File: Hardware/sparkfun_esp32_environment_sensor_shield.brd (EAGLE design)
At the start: 58.4 x 50.8 mm, 51 parts, among them J1 WEATHER_METER-WIND, J2 WEATHER_METER-RAIN, U1 BME280, U2 CCS811, U3 TSL2561FN

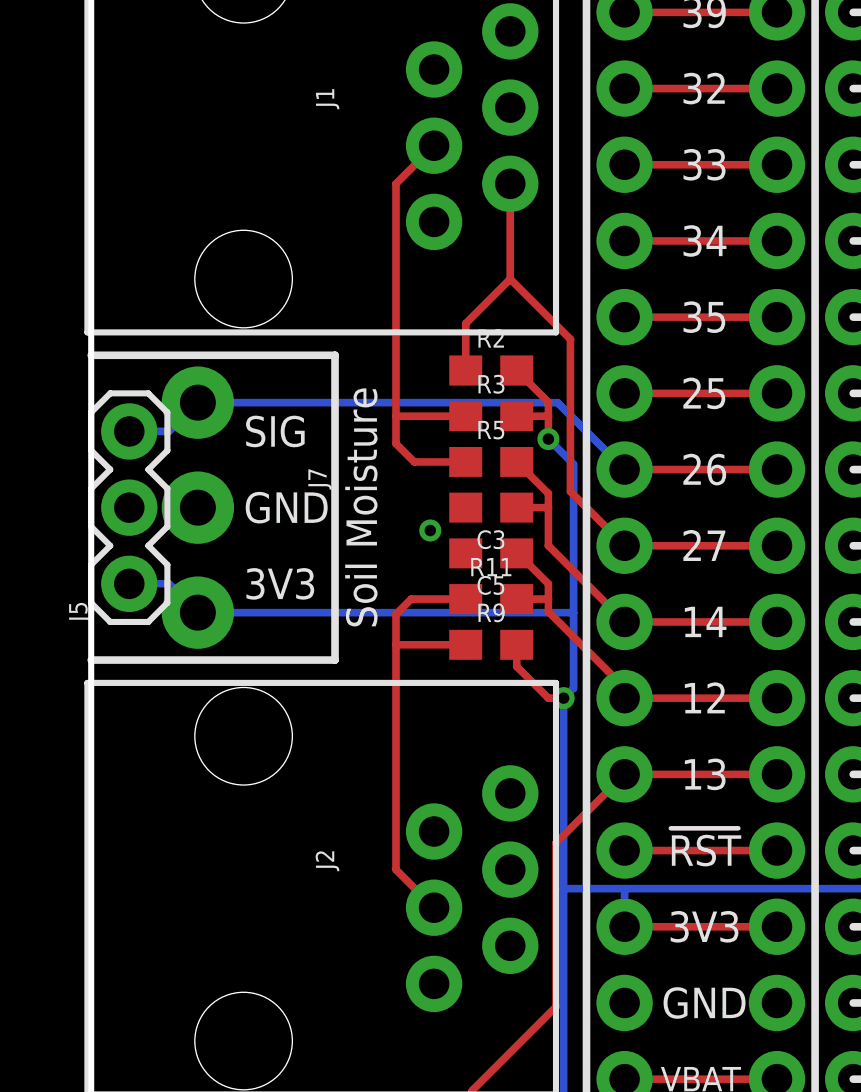
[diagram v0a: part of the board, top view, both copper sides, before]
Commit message: Revising weather meter circuits after tests with ESP32 Thing.
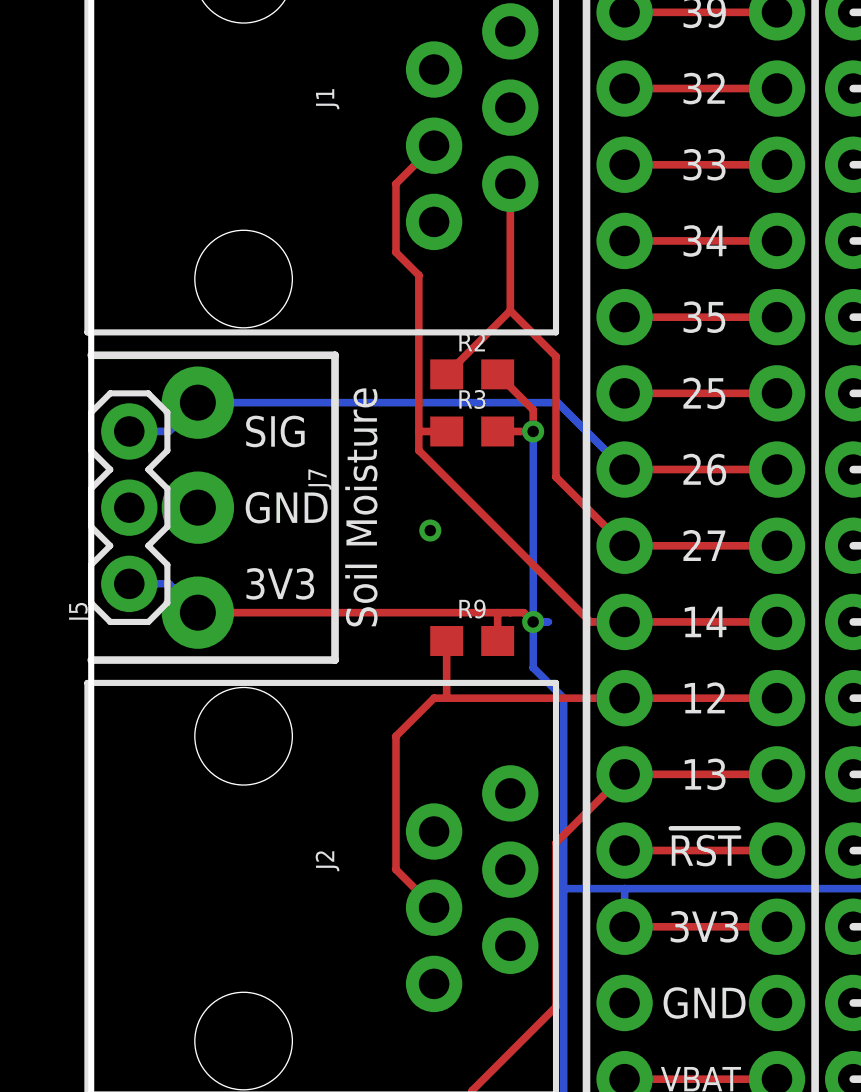
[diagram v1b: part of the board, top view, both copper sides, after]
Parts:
- removed C3, C5: 0.1uF, SparkFun-Capacitors:0603
- removed R11, R5: 330, SparkFun-Resistors:0603
- moved R3 0.81 mm to (12.7, 27.9)
- moved R2 0.65 mm to (12.7, 29.8)
- moved R9 0.65 mm to (12.7, 21.0)
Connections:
- removed net RAIN_OUT: J2.4, R11.1, R9.1
- removed net WIND_OUT: J1.4, R3.1, R5.1
- net GND: no longer C3.2, C5.2
- net RAINFALL: now also J2.4, R9.1; no longer C5.1, R11.2
- net WIND_SPEED: now also J1.4, R3.1; no longer C3.1, R5.2
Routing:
- net WIND_OUT: track 15.4 -> 0.00 mm
- net RAIN_OUT: track 15.2 -> 0.00 mm
- net WIND_SPEED: track 13.0 -> 26.2 mm
- net RAINFALL: track 12.5 -> 21.4 mm
- net 3.3V: track 212.6 -> 210.1 mm
- net WIND_DIR: track 22.4 -> 21.7 mm

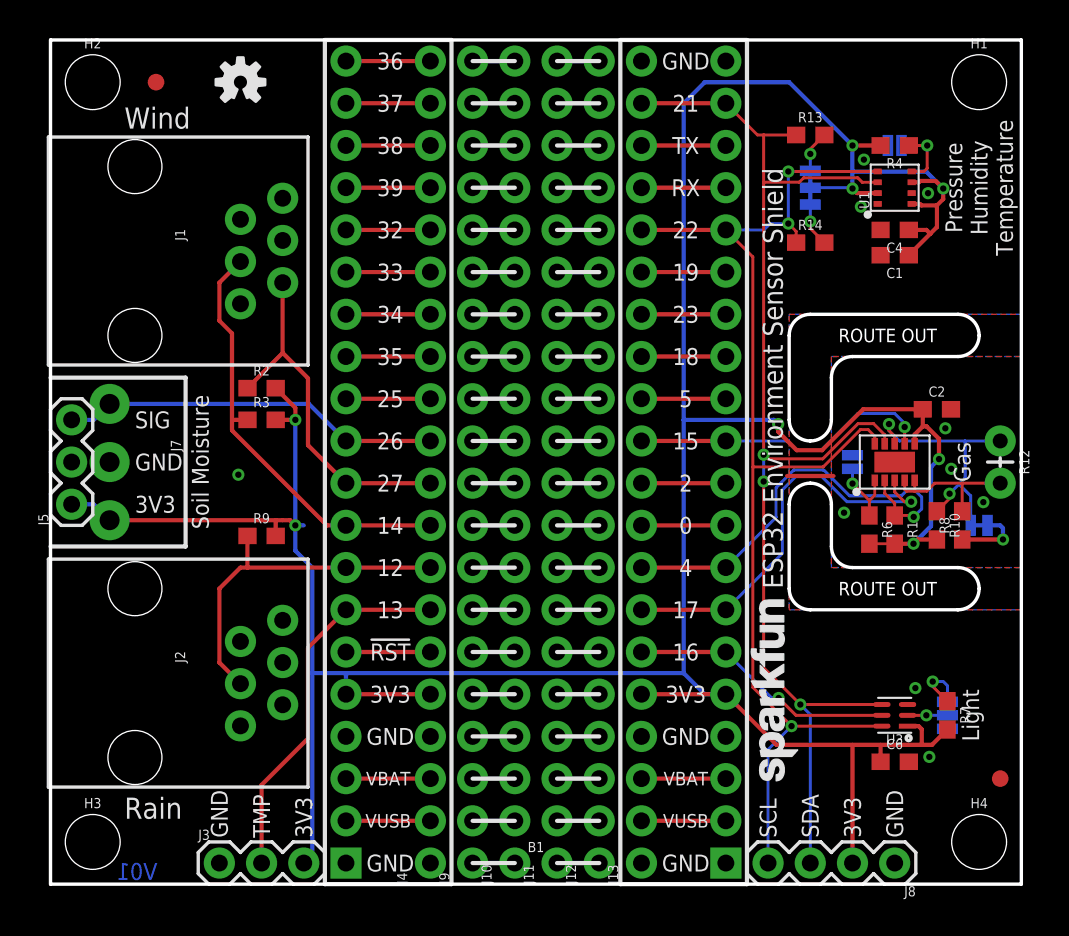
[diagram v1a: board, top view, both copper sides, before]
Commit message: Adding TVS diode to weather meter signals.
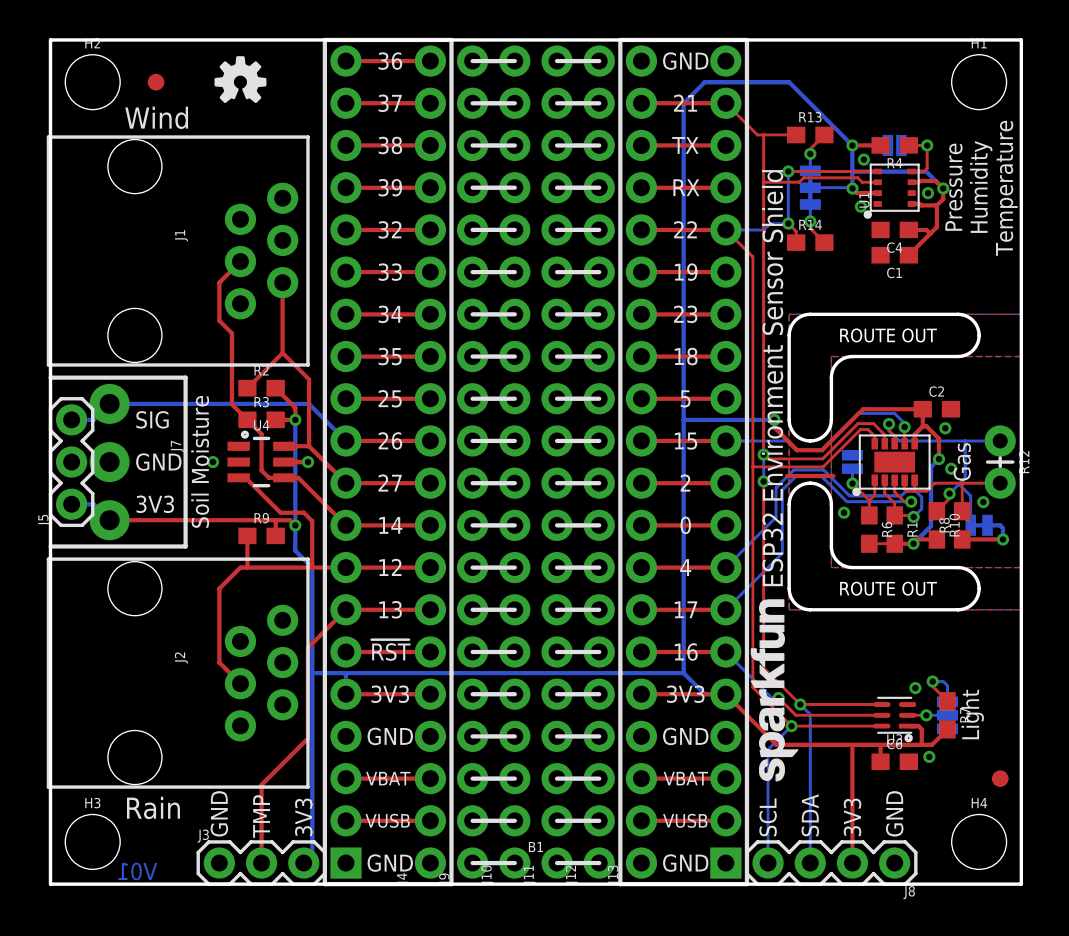
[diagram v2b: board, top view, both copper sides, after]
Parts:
- added U4: ESD Diode, esp32-environ-monitor-temp:SOT-23-6
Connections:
- net 3.3V: now also U4.5
- net GND: now also U4.2
- net RAINFALL: now also U4.3
- net WIND_DIR: now also U4.6
- net WIND_SPEED: now also U4.4
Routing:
- net RAINFALL: track 21.4 -> 29.7 mm
- net 3.3V: track 210.1 -> 211.8 mm, vias 8 -> 9
- net WIND_DIR: track 21.7 -> 23.2 mm
- net WIND_SPEED: track 26.2 -> 25.7 mm
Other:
- board text added: "LUX !INT!"
- board text removed: "LUX-INT"
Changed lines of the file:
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@@
 <text x="41.783" y="16.51" size="0.889" layer="22" font="vector" ratio="15" rot="MR0" align="center-right">GAS
 !INT!</text>
-<text x="41.656" y="13.97" size="0.889" layer="22" font="vector" ratio="15" rot="MR0" align="center-right">LUX-INT</text>
+<text x="41.656" y="13.97" size="0.889" layer="22" font="vector" ratio="15" rot="MR0" align="center-right">LUX
+!INT!</text>
 <text x="41.783" y="19.05" size="0.889" layer="22" font="vector" ratio="15" rot="MR0" align="center-right">GAS
 !RST!</text>
@@
 <element name="FD1" library="SparkFun-Aesthetics" package="FIDUCIAL-1X2" value="FIDUCIAL1X2" x="6.35" y="48.26"/>
 <element name="FD2" library="SparkFun-Aesthetics" package="FIDUCIAL-1X2" value="FIDUCIAL1X2" x="57.15" y="6.35"/>
+<element name="U4" library="esp32-environ-monitor-temp" package="SOT-23-6" value="ESD Diode" x="12.7" y="25.4" rot="R270">
+<attribute name="PROD_ID" value="IC-13538" x="12.7" y="25.4" size="0.889" layer="27" font="vector" ratio="15" rot="R270" display="off"/>
+</element>
 </elements>
 <signals>
@@
 <via x="52.8828" y="7.6581" extent="1-16" drill="0.381"/>
 <via x="52.0446" y="11.7983" extent="1-16" drill="0.381"/>
-<via x="11.303" y="24.638" extent="1-16" drill="0.381"/>
+<contactref element="U4" pad="2"/>
+<via x="9.779" y="25.4" extent="1-16" drill="0.381"/>
 </signal>
 <signal name="SCL">
@@
 <wire x1="43.1673" y1="25.5905" x2="42.9133" y2="25.8445" width="0.1778" layer="1"/>
 <wire x1="42.9133" y1="13.0175" x2="42.9133" y2="24.2316" width="0.1778" layer="1"/>
-<wire x1="42.9133" y1="25.8445" x2="42.9133" y2="42.2148" width="0.1778" layer="1"/>
+<wire x1="42.9133" y1="25.8445" x2="42.9133" y2="42.2402" width="0.1778" layer="1"/>
 <wire x1="42.9133" y1="42.2402" x2="42.9133" y2="45.085" width="0.1778" layer="1"/>
 <wire x1="42.9133" y1="45.085" x2="42.545" y2="45.085" width="0.1778" layer="1"/>
@@
 <wire x1="45.3263" y1="42.5069" x2="45.0596" y2="42.2402" width="0.1778" layer="1"/>
 <wire x1="45.0596" y1="42.2402" x2="42.9133" y2="42.2402" width="0.1778" layer="1"/>
-<wire x1="42.9133" y1="42.2402" x2="42.9133" y2="42.2148" width="0.1778" layer="1"/>
 </signal>
 <signal name="3.3V">
@@
 <wire x1="52" y1="26.5" x2="52" y2="27.0572" width="0.254" layer="1"/>
 <wire x1="50.8" y1="20.486" x2="51.9312" y2="20.486" width="0.254" layer="1"/>
-<via x="43.7896" y="27.686" extent="1-16" drill="0.381"/>
+<via x="43.561" y="27.94" extent="1-16" drill="0.381"/>
 <wire x1="38.1" y1="12.7" x2="39.37" y2="11.43" width="0.254" layer="16"/>
 <wire x1="39.37" y1="11.43" x2="40.64" y2="11.43" width="0.254" layer="16"/>
@@
 <wire x1="52.4256" y1="8.4074" x2="52.4002" y2="8.382" width="0.254" layer="1"/>
 <wire x1="52.9844" y1="21.5392" x2="51.9312" y2="20.486" width="0.254" layer="16"/>
-<wire x1="46.4312" y1="26.1112" x2="44.9072" y2="26.1112" width="0.254" layer="1"/>
-<wire x1="44.9072" y1="26.1112" x2="43.7896" y2="27.2288" width="0.254" layer="1"/>
-<wire x1="43.7896" y1="27.2288" x2="43.7896" y2="27.686" width="0.254" layer="1"/>
-<wire x1="43.7896" y1="27.686" x2="43.5356" y2="27.94" width="0.254" layer="16"/>
-<wire x1="43.5356" y1="27.94" x2="38.1" y2="27.94" width="0.254" layer="16"/>
+<wire x1="46.4312" y1="26.1112" x2="44.9326" y2="26.1112" width="0.254" layer="1"/>
+<wire x1="44.9326" y1="26.1112" x2="43.561" y2="27.4828" width="0.254" layer="1"/>
+<wire x1="43.561" y1="27.4828" x2="43.561" y2="27.94" width="0.254" layer="1"/>
+<wire x1="43.561" y1="27.94" x2="38.1" y2="27.94" width="0.254" layer="16"/>
 <via x="14.732" y="27.94" extent="1-16" drill="0.381"/>
 <wire x1="14.732" y1="27.94" x2="13.55" y2="27.94" width="0.254" layer="1"/>
-<wire x1="14.732" y1="21.59" x2="14.732" y2="27.94" width="0.254" layer="16"/>
+<wire x1="14.732" y1="21.59" x2="14.732" y2="25.4" width="0.254" layer="16"/>
+<wire x1="14.732" y1="25.4" x2="14.732" y2="27.94" width="0.254" layer="16"/>
 <wire x1="14.732" y1="27.94" x2="14.732" y2="28.663" width="0.254" layer="1"/>
 <wire x1="14.732" y1="28.663" x2="13.55" y2="29.845" width="0.254" layer="1"/>
@@
 <wire x1="14.732" y1="20.066" x2="14.732" y2="21.59" width="0.254" layer="16"/>
 <wire x1="3.556" y1="21.9" x2="13.55" y2="21.9" width="0.254" layer="1"/>
-<wire x1="13.97" y1="21.9" x2="14.422" y2="21.9" width="0.254" layer="1"/>
+<wire x1="13.55" y1="21.9" x2="14.422" y2="21.9" width="0.254" layer="1"/>
 <wire x1="14.422" y1="21.9" x2="14.732" y2="21.59" width="0.254" layer="1"/>
 <via x="14.732" y="21.59" extent="1-16" drill="0.381"/>
-<wire x1="14.732" y1="21.59" x2="15.24" y2="21.59" width="0.254" layer="16"/>
 <wire x1="13.55" y1="20.955" x2="13.55" y2="21.9" width="0.254" layer="1"/>
-<wire x1="13.55" y1="21.9" x2="13.97" y2="21.9" width="0.254" layer="1"/>
+<contactref element="U4" pad="5"/>
+<wire x1="14.0751" y1="25.4" x2="15.494" y2="25.4" width="0.254" layer="1"/>
+<via x="15.494" y="25.4" extent="1-16" drill="0.381"/>
+<wire x1="15.494" y1="25.4" x2="14.732" y2="25.4" width="0.254" layer="16"/>
 </signal>
 <signal name="ADDR_TSL2561">
@@
 <contactref element="J4" pad="10"/>
 <wire x1="22.86" y1="24.13" x2="17.78" y2="24.13" width="0.254" layer="1"/>
-<wire x1="17.78" y1="24.13" x2="15.494" y2="26.416" width="0.254" layer="1"/>
 <wire x1="13.97" y1="31.965" x2="13.97" y2="36.195" width="0.254" layer="1"/>
 <wire x1="11.85" y1="29.845" x2="13.97" y2="31.965" width="0.254" layer="1"/>
-<wire x1="13.97" y1="31.965" x2="15.494" y2="30.441" width="0.254" layer="1"/>
-<wire x1="15.494" y1="30.441" x2="15.494" y2="26.416" width="0.254" layer="1"/>
+<wire x1="13.97" y1="31.965" x2="15.56" y2="30.375" width="0.254" layer="1"/>
+<wire x1="17.78" y1="24.13" x2="15.56" y2="26.35" width="0.254" layer="1"/>
+<contactref element="U4" pad="6"/>
+<wire x1="15.56" y1="26.67" x2="15.56" y2="30.375" width="0.254" layer="1"/>
+<wire x1="14.0751" y1="26.35" x2="15.56" y2="26.35" width="0.254" layer="1"/>
+<wire x1="15.56" y1="26.35" x2="15.56" y2="26.67" width="0.254" layer="1"/>
 </signal>
 <signal name="WIND_SPEED">
@@
 <contactref element="J1" pad="4"/>
 <contactref element="R3" pad="1"/>
-<wire x1="17.78" y1="21.59" x2="16.637" y2="21.59" width="0.254" layer="1"/>
-<wire x1="16.637" y1="21.59" x2="10.922" y2="27.305" width="0.254" layer="1"/>
-<wire x1="10.922" y1="27.305" x2="10.922" y2="27.94" width="0.254" layer="1"/>
-<wire x1="10.922" y1="27.94" x2="10.922" y2="33.147" width="0.254" layer="1"/>
 <wire x1="10.922" y1="33.147" x2="10.16" y2="33.909" width="0.254" layer="1"/>
 <wire x1="10.16" y1="33.909" x2="10.16" y2="36.195" width="0.254" layer="1"/>
 <wire x1="10.16" y1="36.195" x2="11.43" y2="37.465" width="0.254" layer="1"/>
-<wire x1="11.85" y1="27.94" x2="10.922" y2="27.94" width="0.254" layer="1"/>
+<contactref element="U4" pad="4"/>
+<wire x1="11.85" y1="27.94" x2="10.922" y2="28.868" width="0.254" layer="1"/>
+<wire x1="10.922" y1="28.868" x2="10.922" y2="33.147" width="0.254" layer="1"/>
+<wire x1="17.78" y1="21.59" x2="14.92" y2="24.45" width="0.254" layer="1"/>
+<wire x1="14.92" y1="24.45" x2="14.0751" y2="24.45" width="0.254" layer="1"/>
+<wire x1="14.0751" y1="24.45" x2="13.142" y2="24.45" width="0.254" layer="1"/>
+<wire x1="13.142" y1="24.45" x2="12.7" y2="24.892" width="0.254" layer="1"/>
+<wire x1="12.7" y1="24.892" x2="12.7" y2="27.09" width="0.254" layer="1"/>
+<wire x1="12.7" y1="27.09" x2="11.85" y2="27.94" width="0.254" layer="1"/>
 </signal>
 <signal name="RAINFALL">
@@
 <contactref element="J2" pad="4"/>
 <contactref element="R9" pad="1"/>
-<wire x1="17.78" y1="19.05" x2="11.85" y2="19.05" width="0.254" layer="1"/>
+<wire x1="17.78" y1="19.05" x2="15.748" y2="19.05" width="0.254" layer="1"/>
+<wire x1="15.748" y1="19.05" x2="11.85" y2="19.05" width="0.254" layer="1"/>
 <wire x1="11.43" y1="19.05" x2="10.16" y2="17.78" width="0.254" layer="1"/>
 <wire x1="10.16" y1="17.78" x2="10.16" y2="13.335" width="0.254" layer="1"/>
@@
 <wire x1="11.85" y1="20.955" x2="11.85" y2="19.05" width="0.254" layer="1"/>
 <wire x1="11.85" y1="19.05" x2="11.43" y2="19.05" width="0.254" layer="1"/>
+<wire x1="11.745" y1="24.45" x2="13.843" y2="22.352" width="0.254" layer="1"/>
+<wire x1="13.843" y1="22.352" x2="15.24" y2="22.352" width="0.254" layer="1"/>
+<wire x1="15.24" y1="22.352" x2="15.748" y2="21.844" width="0.254" layer="1"/>
+<wire x1="15.748" y1="21.844" x2="15.748" y2="19.05" width="0.254" layer="1"/>
+<contactref element="U4" pad="3"/>
+<wire x1="11.745" y1="24.45" x2="11.3249" y2="24.45" width="0.254" layer="1"/>
 </signal>
 <signal name="EXT_TEMPERATURE">
